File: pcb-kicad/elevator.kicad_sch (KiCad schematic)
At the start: 155 parts, among them Q1 AO3416, SW1 MX-with-LED, SW10 MX-with-LED, SW11 MX-with-LED, SW12 MX-with-LED, SW13 MX-with-LED, SW14 MX-with-LED, SW15 MX-with-LED, SW16 MX-with-LED, SW17 MX-with-LED, SW18 MX-with-LED, SW19 MX-with-LED, SW2 MX-with-LED, SW20 MX-with-LED, SW21 MX-with-LED, SW22 MX-with-LED, SW23 MX-with-LED, SW24 MX-with-LED, SW25 MX-with-LED, SW26 MX-with-LED, SW27 MX-with-LED, SW28 MX-with-LED, SW29 MX-with-LED, SW3 MX-with-LED, SW30 MX-with-LED, SW31 MX-with-LED, SW32 MX-with-LED, SW33 MX-with-LED, SW34 MX-with-LED, SW35 MX-with-LED, SW36 MX-with-LED, SW37 MX-with-LED, SW38 MX-with-LED, SW39 MX-with-LED, SW4 MX-with-LED, SW40 MX-with-LED, SW41 MX-with-LED, SW42 MX-with-LED, SW43 MX-with-LED, SW44 MX-with-LED, SW45 MX-with-LED, SW46 MX-with-LED, SW47 MX-with-LED, SW48 MX-with-LED, SW49 RotaryEncoder_Switch, SW5 MX-with-LED, SW6 MX-with-LED, SW7 MX-with-LED, SW8 MX-with-LED, SW9 MX-with-LED, U1 Frood

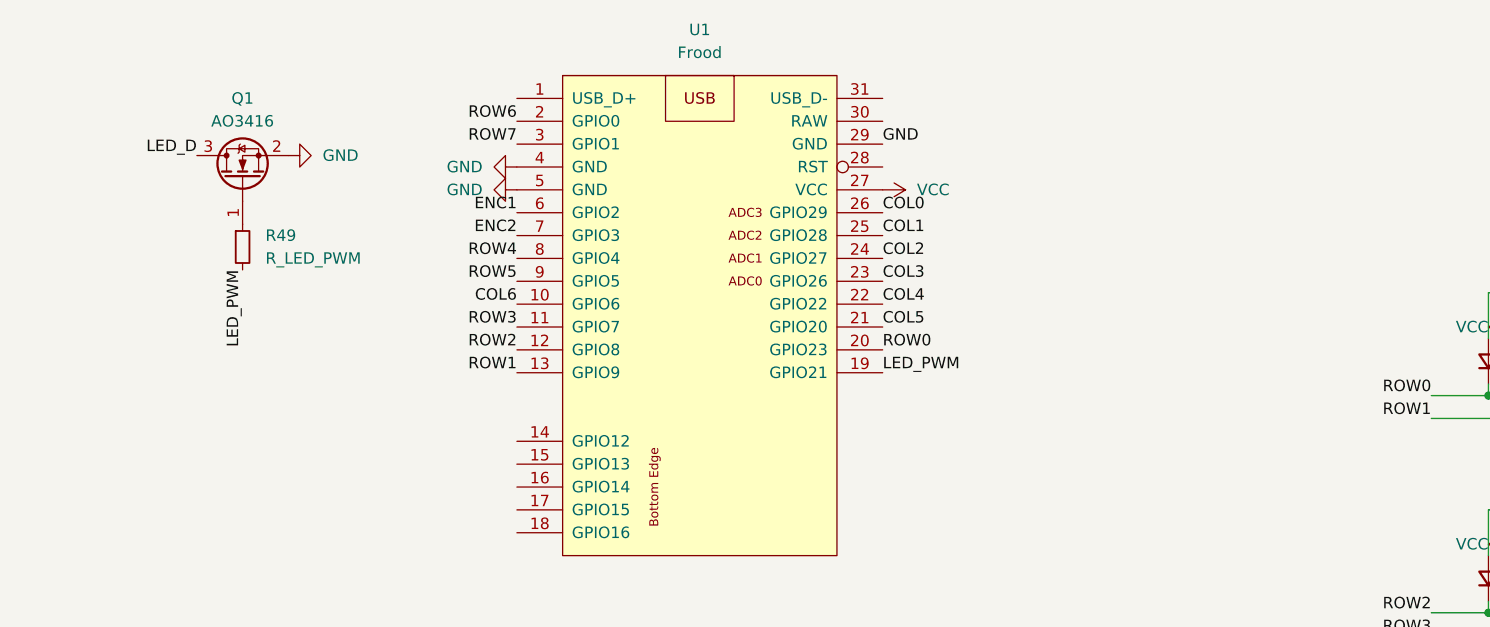
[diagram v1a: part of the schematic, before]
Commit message: Add ledstrip circuitry to schematic
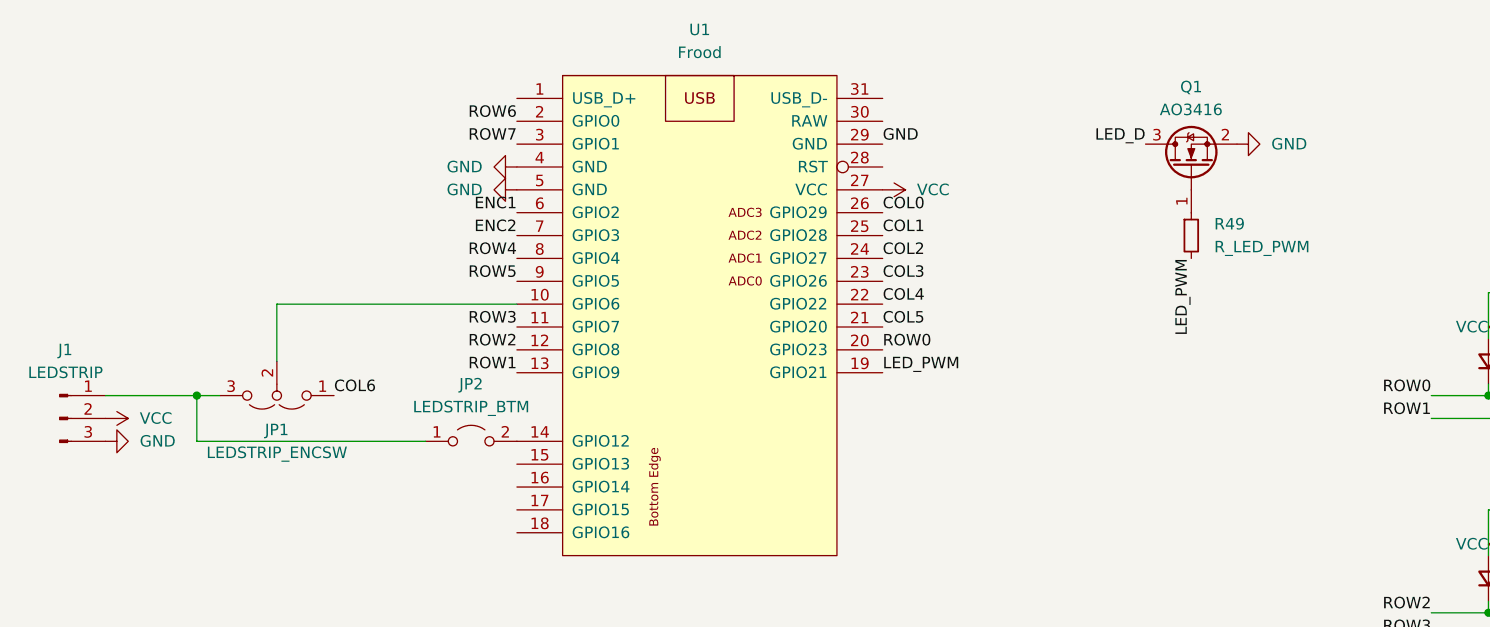
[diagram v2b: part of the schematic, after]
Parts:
- added J1: LEDSTRIP, symbol Connector:Conn_01x03_Pin
- added JP1: LEDSTRIP_ENCSW, symbol Jumper:Jumper_3_Open
- added JP2: LEDSTRIP_BTM, symbol Jumper:Jumper_2_Open
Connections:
- net COL6: now also JP1.1 (A); no longer U1.10 (GPIO6)
- net GND: now also J1.3 (Pin_3)
- net VCC: now also J1.2 (Pin_2)
- net at U1.14 (GPIO12): now also JP2.2 (B)
- new net: JP1.2 (C), U1.10 (GPIO6)
- new net: J1.1 (Pin_1), JP1.3 (B), JP2.1 (A)
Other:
- moved on the sheet: Q1, R49
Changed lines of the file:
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@@
   (junction (at 401.32 71.12) (diameter 0) (color 0 0 0 0)
   )
+  (junction (at 33.02 58.42) (diameter 0) (color 0 0 0 0)
+  )
   (junction (at 176.53 105.41) (diameter 0) (color 0 0 0 0)
   )
@@
     (stroke (width 0) (type default))
   )
+  (wire (pts (xy 33.02 58.42) (xy 35.56 58.42))
+    (stroke (width 0) (type default))
+  )
   (wire (pts (xy 360.68 46.99) (xy 363.22 46.99))
     (stroke (width 0) (type default))
@@
     (stroke (width 0) (type default))
   )
+  (wire (pts (xy 22.86 58.42) (xy 33.02 58.42))
+    (stroke (width 0) (type default))
+  )
   (wire (pts (xy 255.27 93.98) (xy 252.73 93.98))
     (stroke (width 0) (type default))
@@
     (stroke (width 0) (type default))
   )
+  (wire (pts (xy 58.42 63.5) (xy 33.02 63.5))
+    (stroke (width 0) (type default))
+  )
   (wire (pts (xy 287.02 38.1) (xy 287.02 46.99))
     (stroke (width 0) (type default))
@@
     (stroke (width 0) (type default))
   )
+  (wire (pts (xy 41.91 48.26) (xy 68.58 48.26))
+    (stroke (width 0) (type default))
+  )
   (wire (pts (xy 344.17 71.12) (xy 344.17 93.98))
     (stroke (width 0) (type default))
@@
     (stroke (width 0) (type default))
   )
+  (wire (pts (xy 33.02 63.5) (xy 33.02 58.42))
+    (stroke (width 0) (type default))
+  )
   (wire (pts (xy 252.73 93.98) (xy 252.73 99.06))
     (stroke (width 0) (type default))
@@
     (stroke (width 0) (type default))
   )
+  (wire (pts (xy 41.91 48.26) (xy 41.91 54.61))
+    (stroke (width 0) (type default))
+  )
   (wire (pts (xy 265.43 46.99) (xy 267.97 46.99))
     (stroke (width 0) (type default))
@@
     (effects (font (size 1.27 1.27)) (justify right bottom))
   )
-  (label "LED_D" (at 33.02 31.75 180) (fields_autoplaced)
+  (label "LED_D" (at 138.43 30.48 180) (fields_autoplaced)
     (effects (font (size 1.27 1.27)) (justify right bottom))
   )
@@
     (effects (font (size 1.27 1.27)) (justify left bottom))
   )
-  (label "LED_PWM" (at 38.1 44.45 270) (fields_autoplaced)
+  (label "LED_PWM" (at 143.51 43.18 270) (fields_autoplaced)
     (effects (font (size 1.27 1.27)) (justify right bottom))
   )
@@
     (effects (font (size 1.27 1.27)) (justify right bottom))
   )
+  (label "COL6" (at 48.26 58.42 0) (fields_autoplaced)
+    (effects (font (size 1.27 1.27)) (justify left bottom))
+  )
   (label "GND" (at 109.22 30.48 0) (fields_autoplaced)
     (effects (font (size 1.27 1.27)) (justify left bottom))
@@
     (effects (font (size 1.27 1.27)) (justify right bottom))
   )
-  (label "COL6" (at 68.58 48.26 180) (fields_autoplaced)
-    (effects (font (size 1.27 1.27)) (justify right bottom))
-  )
   (label "ROW5" (at 170.18 107.95 180) (fields_autoplaced)
     (effects (font (size 1.27 1.27)) (justify right bottom))
@@
     )
   )
-  (symbol (lib_id "Device:R_Small") (at 38.1 41.91 0) (unit 1)
+  (symbol (lib_id "Device:R_Small") (at 143.51 40.64 0) (unit 1)
     (in_bom yes) (on_board yes) (dnp no) (fields_autoplaced)
-    (property "Reference" "R49" (at 40.64 40.64 0)
+    (property "Reference" "R49" (at 146.05 39.37 0)
       (effects (font (size 1.27 1.27)) (justify left))
     )
-    (property "Value" "R_LED_PWM" (at 40.64 43.18 0)
+    (property "Value" "R_LED_PWM" (at 146.05 41.91 0)
       (effects (font (size 1.27 1.27)) (justify left))
     )
-    (property "Footprint" "Keebio-Parts:Resistor-Hybrid" (at 38.1 41.91 0)
+    (property "Footprint" "Keebio-Parts:Resistor-Hybrid" (at 143.51 40.64 0)
       (effects (font (size 1.27 1.27)) hide)
     )
-    (property "Datasheet" "~" (at 38.1 41.91 0)
+    (property "Datasheet" "~" (at 143.51 40.64 0)
       (effects (font (size 1.27 1.27)) hide)
     )
@@
     )
   )
+  (symbol (lib_id "power:GND") (at 22.86 63.5 90) (unit 1)
+    (in_bom yes) (on_board yes) (dnp no) (fields_autoplaced)
+    (property "Reference" "#PWR059" (at 29.21 63.5 0)
+      (effects (font (size 1.27 1.27)) hide)
+    )
+    (property "Value" "GND" (at 26.67 63.5 90)
+      (effects (font (size 1.27 1.27)) (justify right))
+    )
+    (property "Footprint" "" (at 22.86 63.5 0)
+      (effects (font (size 1.27 1.27)) hide)
+    )
+    (property "Datasheet" "" (at 22.86 63.5 0)
+      (effects (font (size 1.27 1.27)) hide)
+    )
+    (pin "1")
+    (instances
+      (project "elevator"
+        (path "/ec52aef2-1869-4a70-a72a-c2d0a3ee9ccf"
+          (reference "#PWR059") (unit 1)
+        )
+      )
+    )
+  )
   (symbol (lib_id "Device:D_Small") (at 195.58 78.74 90) (unit 1)
     (in_bom yes) (on_board yes) (dnp no) (fields_autoplaced)
@@
     )
   )
-  (symbol (lib_id "power:GND") (at 43.18 31.75 90) (unit 1)
+  (symbol (lib_id "power:GND") (at 148.59 30.48 90) (unit 1)
     (in_bom yes) (on_board yes) (dnp no) (fields_autoplaced)
-    (property "Reference" "#PWR08" (at 49.53 31.75 0)
+    (property "Reference" "#PWR08" (at 154.94 30.48 0)
       (effects (font (size 1.27 1.27)) hide)
     )
-    (property "Value" "GND" (at 46.99 31.75 90)
+    (property "Value" "GND" (at 152.4 30.48 90)
       (effects (font (size 1.27 1.27)) (justify right))
     )
-    (property "Footprint" "" (at 43.18 31.75 0)
+    (property "Footprint" "" (at 148.59 30.48 0)
       (effects (font (size 1.27 1.27)) hide)
     )
-    (property "Datasheet" "" (at 43.18 31.75 0)
+    (property "Datasheet" "" (at 148.59 30.48 0)
       (effects (font (size 1.27 1.27)) hide)
     )
@@
     )
   )
+  (symbol (lib_id "power:VCC") (at 22.86 60.96 270) (unit 1)
+    (in_bom yes) (on_board yes) (dnp no) (fields_autoplaced)
+    (property "Reference" "#PWR058" (at 19.05 60.96 0)
+      (effects (font (size 1.27 1.27)) hide)
+    )
+    (property "Value" "VCC" (at 26.67 60.96 90)
+      (effects (font (size 1.27 1.27)) (justify left))
+    )
+    (property "Footprint" "" (at 22.86 60.96 0)
+      (effects (font (size 1.27 1.27)) hide)
+    )
+    (property "Datasheet" "" (at 22.86 60.96 0)
+      (effects (font (size 1.27 1.27)) hide)
+    )
+    (pin "1")
+    (instances
+      (project "elevator"
+        (path "/ec52aef2-1869-4a70-a72a-c2d0a3ee9ccf"
+          (reference "#PWR058") (unit 1)
+        )
+      )
+    )
+  )
   (symbol (lib_id "keebio:MX-with-LED") (at 374.65 118.11 0) (unit 1)
     (in_bom yes) (on_board yes) (dnp no) (fields_autoplaced)
@@
     )
   )
+  (symbol (lib_id "Jumper:Jumper_3_Open") (at 41.91 58.42 180) (unit 1)
+    (in_bom yes) (on_board yes) (dnp no) (fields_autoplaced)
+    (property "Reference" "JP1" (at 41.91 62.23 0)
+      (effects (font (size 1.27 1.27)))
+    )
+    (property "Value" "LEDSTRIP_ENCSW" (at 41.91 64.77 0)
+      (effects (font (size 1.27 1.27)))
+    )
+    (property "Footprint" "" (at 41.91 58.42 0)
+      (effects (font (size 1.27 1.27)) hide)
+    )
+    (property "Datasheet" "~" (at 41.91 58.42 0)
+      (effects (font (size 1.27 1.27)) hide)
+    )
+    (pin "3")
+    (pin "2")
+    (pin "1")
+    (instances
+      (project "elevator"
+        (path "/ec52aef2-1869-4a70-a72a-c2d0a3ee9ccf"
+          (reference "JP1") (unit 1)
+        )
+      )
+    )
+  )
   (symbol (lib_id "power:VCC") (at 128.27 128.27 0) (unit 1)
     (in_bom yes) (on_board yes) (dnp no) (fields_autoplaced)
@@
     )
   )
+  (symbol (lib_id "Connector:Conn_01x03_Pin") (at 17.78 60.96 0) (unit 1)
+    (in_bom yes) (on_board yes) (dnp no) (fields_autoplaced)
+    (property "Reference" "J1" (at 18.415 53.34 0)
+      (effects (font (size 1.27 1.27)))
+    )
+    (property "Value" "LEDSTRIP" (at 18.415 55.88 0)
+      (effects (font (size 1.27 1.27)))
+    )
+    (property "Footprint" "" (at 17.78 60.96 0)
+      (effects (font (size 1.27 1.27)) hide)
+    )
+    (property "Datasheet" "~" (at 17.78 60.96 0)
+      (effects (font (size 1.27 1.27)) hide)
+    )
+    (pin "2")
+    (pin "3")
+    (pin "1")
+    (instances
+      (project "elevator"
+        (path "/ec52aef2-1869-4a70-a72a-c2d0a3ee9ccf"
+          (reference "J1") (unit 1)
+        )
+      )
+    )
+  )
   (symbol (lib_id "power:GND") (at 68.58 33.02 270) (unit 1)
     (in_bom yes) (on_board yes) (dnp no) (fields_autoplaced)
@@
     )
   )
+  (symbol (lib_id "Jumper:Jumper_2_Open") (at 63.5 63.5 0) (unit 1)
+    (in_bom yes) (on_board yes) (dnp no) (fields_autoplaced)
+    (property "Reference" "JP2" (at 63.5 57.15 0)
+      (effects (font (size 1.27 1.27)))
+    )
+    (property "Value" "LEDSTRIP_BTM" (at 63.5 59.69 0)
+      (effects (font (size 1.27 1.27)))
+    )
+    (property "Footprint" "" (at 63.5 63.5 0)
+      (effects (font (size 1.27 1.27)) hide)
+    )
+    (property "Datasheet" "~" (at 63.5 63.5 0)
+      (effects (font (size 1.27 1.27)) hide)
+    )
+    (pin "1")
+    (pin "2")
+    (instances
+      (project "elevator"
+        (path "/ec52aef2-1869-4a70-a72a-c2d0a3ee9ccf"
+          (reference "JP2") (unit 1)
+        )
+      )
+    )
+  )
   (symbol (lib_id "power:VCC") (at 179.07 97.79 90) (unit 1)
     (in_bom yes) (on_board yes) (dnp no)
@@
     )
   )
-  (symbol (lib_id "Transistor_FET:AO3400A") (at 38.1 34.29 90) (unit 1)
+  (symbol (lib_id "Transistor_FET:AO3400A") (at 143.51 33.02 90) (unit 1)
     (in_bom yes) (on_board yes) (dnp no) (fields_autoplaced)
-    (property "Reference" "Q1" (at 38.1 25.4 90)
+    (property "Reference" "Q1" (at 143.51 24.13 90)
       (effects (font (size 1.27 1.27)))
     )
-    (property "Value" "AO3416" (at 38.1 27.94 90)
+    (property "Value" "AO3416" (at 143.51 26.67 90)
       (effects (font (size 1.27 1.27)))
     )
-    (property "Footprint" "Package_TO_SOT_SMD:SOT-23" (at 40.005 29.21 0)
+    (property "Footprint" "Package_TO_SOT_SMD:SOT-23" (at 145.415 27.94 0)
       (effects (font (size 1.27 1.27) italic) (justify left) hide)
     )
-    (property "Datasheet" "http://www.aosmd.com/pdfs/datasheet/AO3400A.pdf" (at 41.91 29.21 0)
+    (property "Datasheet" "http://www.aosmd.com/pdfs/datasheet/AO3400A.pdf" (at 147.32 27.94 0)
       (effects (font (size 1.27 1.27)) (justify left) hide)
     )
